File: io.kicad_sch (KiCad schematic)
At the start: 39 parts, among them Q1 BC817, SW1 RotaryEncoder_Switch_MP, SW2 RotaryEncoder_Switch_MP, U1 MAX7221xWG, U2 74HC595, U3 CC56-12GWA, U4 CC56-12GWA

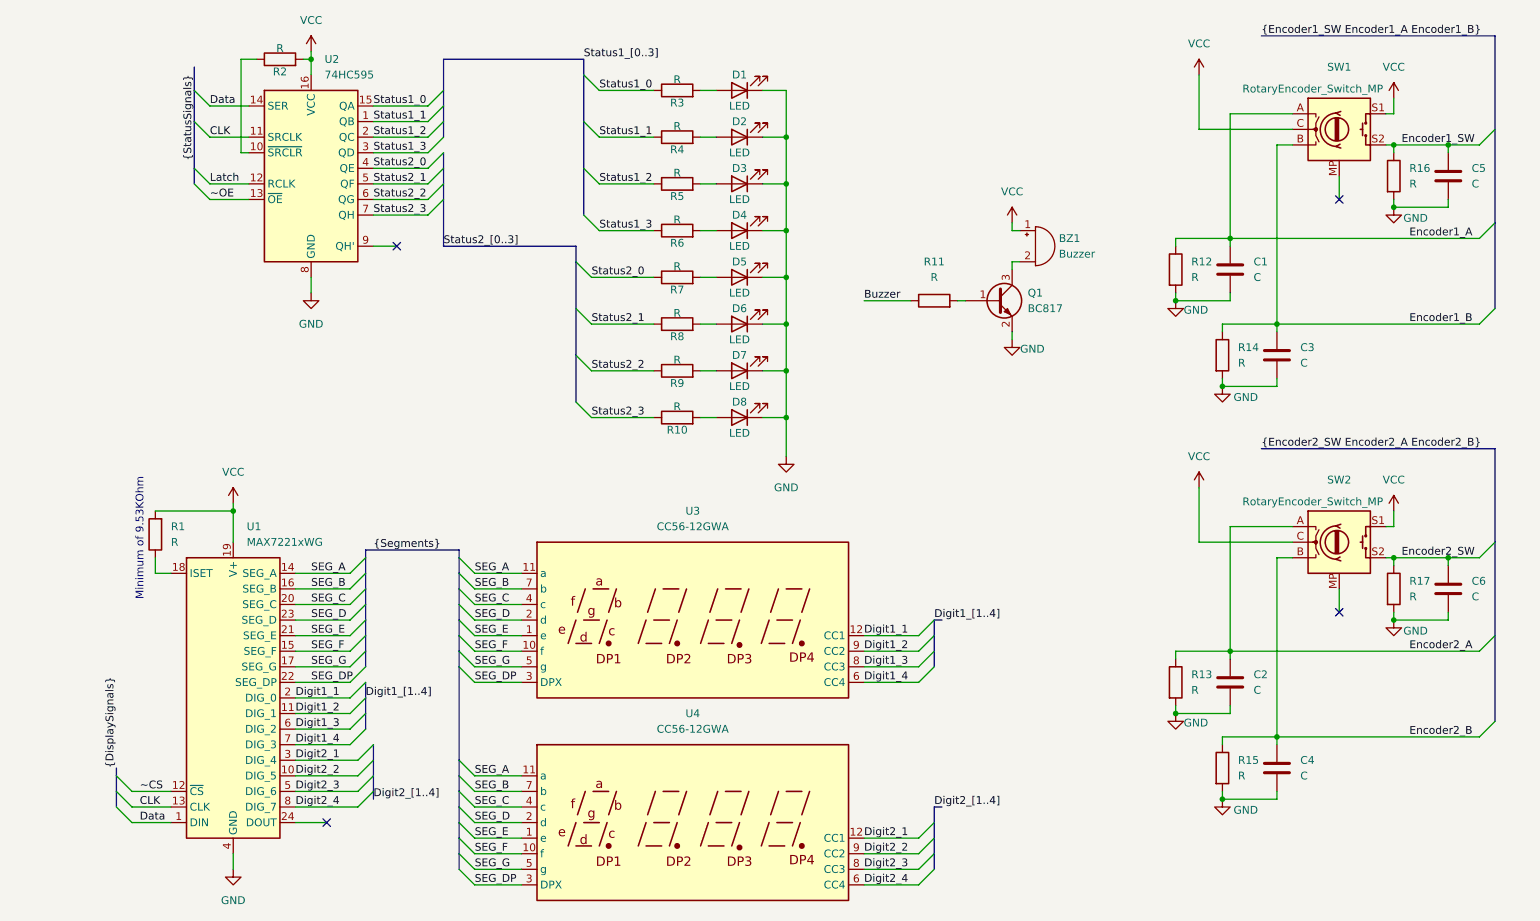
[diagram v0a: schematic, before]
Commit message: Constant current sink status driver
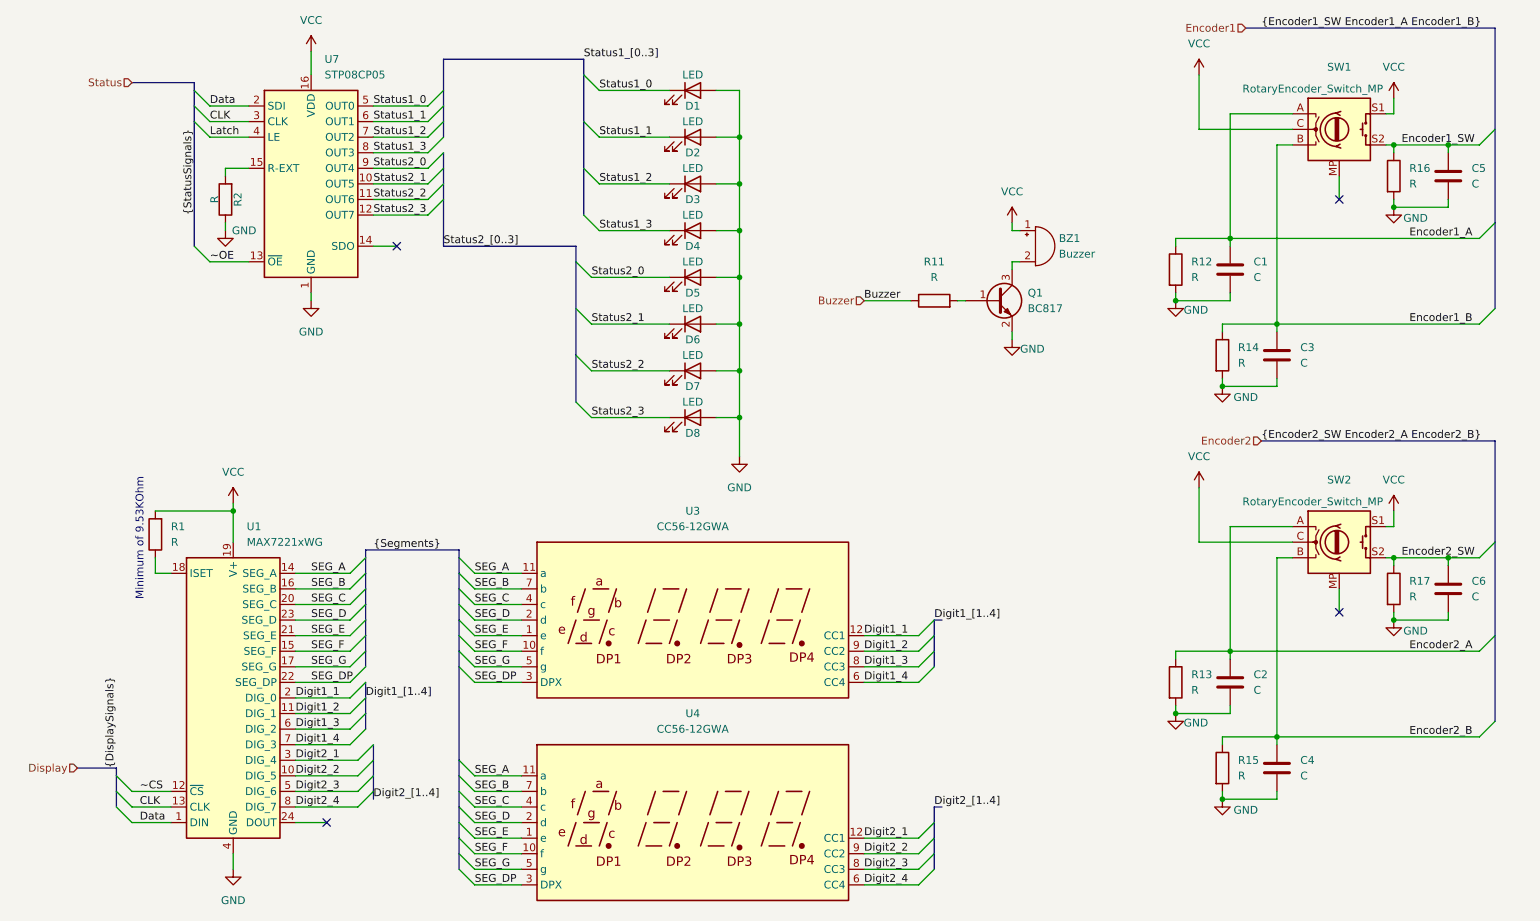
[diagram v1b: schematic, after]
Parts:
- removed R10, R3, R4, R5, R6, R7, R8, R9: R, symbol Device:R
- removed U2: 74HC595, symbol 74xx:74HC595
- added U7: STP08CP05, symbol Driver_LED:STP08CP05
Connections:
- net CLK: now also U7.3 (CLK)
- net Data: now also U7.2 (SDI)
- net GND: now also D1.2 (A), D2.2 (A), D3.2 (A), D4.2 (A), D5.2 (A), D6.2 (A), D7.2 (A), D8.2 (A), R2.1, U7.1 (GND); no longer D1.1 (K), D2.1 (K), D3.1 (K), D4.1 (K), D5.1 (K), D6.1 (K), D7.1 (K), D8.1 (K)
- net Latch: now also U7.4 (LE)
- net Status1_0: now also D1.1 (K), U7.5 (OUT0)
- net Status1_1: now also D2.1 (K), U7.6 (OUT1)
- net Status1_2: now also D3.1 (K), U7.7 (OUT2)
- net Status1_3: now also D4.1 (K), U7.8 (OUT3)
- net Status2_0: now also D5.1 (K), U7.9 (OUT4)
- net Status2_1: now also D6.1 (K), U7.10 (OUT5)
- net Status2_2: now also D7.1 (K), U7.11 (OUT6)
- net Status2_3: now also D8.1 (K), U7.12 (OUT7)
- net VCC: now also U7.16 (VDD); no longer R2.2
- net ~OE: now also U7.13 (~{OE})
- new net: R2.2, U7.15 (R-EXT)
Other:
- moved on the sheet: D1, D2, D3, D4, D5, D6, D7, D8

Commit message: Controller selection
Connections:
- net GND: no longer D1.2 (A), D2.2 (A), D3.2 (A), D4.2 (A), D5.2 (A), D6.2 (A), D7.2 (A), D8.2 (A)
- net VCC: now also D1.2 (A), D2.2 (A), D3.2 (A), D4.2 (A), D5.2 (A), D6.2 (A), D7.2 (A), D8.2 (A)
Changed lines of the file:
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@@
 	)
 	(junction
-		(at 129.54 92.71)
-		(diameter 0)
-		(color 0 0 0 0)
-	)
-	(junction
 		(at 209.55 130.81)
 		(diameter 0)
@@
 	)
 	(junction
+		(at 129.54 39.37)
+		(diameter 0)
+		(color 0 0 0 0)
+	)
+	(junction
 		(at 217.17 144.78)
 		(diameter 0)
@@
 		)
 	)
-	(wire
-		(pts
-			(xy 129.54 99.06) (xy 129.54 92.71)
-		)
-		(stroke
-			(width 0)
-			(type default)
-		)
-	)
 	(bus
 		(pts
@@
 	(wire
 		(pts
+			(xy 129.54 36.83) (xy 129.54 39.37)
+		)
+		(stroke
+			(width 0)
+			(type default)
+		)
+	)
+	(wire
+		(pts
 			(xy 236.22 115.57) (xy 236.22 116.84)
 		)
@@
 	)
 	(symbol
+		(lib_id "power:VCC")
+		(at 129.54 36.83 0)
+		(unit 1)
+		(exclude_from_sim no)
+		(in_bom yes)
+		(on_board yes)
+		(dnp no)
+		(fields_autoplaced yes)
+		(property "Reference" "#PWR05"
+			(at 129.54 40.64 0)
+			(effects
+				(font
+					(size 1.27 1.27)
+				)
+				(hide yes)
+			)
+		)
+		(property "Value" "VCC"
+			(at 129.54 31.75 0)
+			(effects
+				(font
+					(size 1.27 1.27)
+				)
+			)
+		)
+		(property "Footprint" ""
+			(at 129.54 36.83 0)
+			(effects
+				(font
+					(size 1.27 1.27)
+				)
+				(hide yes)
+			)
+		)
+		(property "Datasheet" ""
+			(at 129.54 36.83 0)
+			(effects
+				(font
+					(size 1.27 1.27)
+				)
+				(hide yes)
+			)
+		)
+		(property "Description" "Power symbol creates a global label with name \"VCC\""
+			(at 129.54 36.83 0)
+			(effects
+				(font
+					(size 1.27 1.27)
+				)
+				(hide yes)
+			)
+		)
+		(pin "1"
+		)
+		(instances
+			(project "LifeCounter"
+				(path "/16b3e55a-9d75-49bf-a6fe-25414eb3d7da/6b761b5e-3125-4b22-9fe1-2e6b42db1157"
+					(reference "#PWR05")
+					(unit 1)
+				)
+			)
+		)
+	)
+	(symbol
 		(lib_id "Display_Character:CC56-12GWA")
 		(at 121.92 158.75 0)
@@
 					(unit 1)
 				)
-			)
-		)
-	)
-	(symbol
-		(lib_id "power:GND")
-		(at 129.54 99.06 0)
-		(unit 1)
-		(exclude_from_sim no)
-		(in_bom yes)
-		(on_board yes)
-		(dnp no)
-		(fields_autoplaced yes)
-		(property "Reference" "#PWR05"
-			(at 129.54 105.41 0)
-			(effects
-				(font
-					(size 1.27 1.27)
-				)
-				(hide yes)
-			)
-		)
-		(property "Value" "GND"
-			(at 129.54 104.14 0)
-			(effects
-				(font
-					(size 1.27 1.27)
-				)
-			)
-		)
-		(property "Footprint" ""
-			(at 129.54 99.06 0)
-			(effects
-				(font
-					(size 1.27 1.27)
-				)
-				(hide yes)
-			)
-		)
-		(property "Datasheet" ""
-			(at 129.54 99.06 0)
-			(effects
-				(font
-					(size 1.27 1.27)
-				)
-				(hide yes)
-			)
-		)
-		(property "Description" "Power symbol creates a global label with name \"GND\" , ground"
-			(at 129.54 99.06 0)
-			(effects
-				(font
-					(size 1.27 1.27)
-				)
-				(hide yes)
-			)
-		)
-		(pin "1"
-		)
-		(instances
-			(project "LifeCounter"
-				(path "/16b3e55a-9d75-49bf-a6fe-25414eb3d7da/6b761b5e-3125-4b22-9fe1-2e6b42db1157"
-					(reference "#PWR05")
-					(unit 1)
-				)
